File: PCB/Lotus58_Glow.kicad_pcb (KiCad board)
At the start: 2 copper layers, 139.1 x 107.7 mm, 133 parts, among them J1 PJ-320A, J2 Conn_01x02, P1 OLED, SW1 Kailh hotswap MX socket, SW10 Kailh hotswap MX socket, SW11 Kailh hotswap MX socket, SW12 Kailh hotswap MX socket, SW13 Kailh hotswap MX socket, SW14 Kailh hotswap MX socket, SW15 Kailh hotswap MX socket, SW16 Kailh hotswap MX socket, SW17 Kailh hotswap MX socket, SW18 Kailh hotswap MX socket, SW19 Kailh hotswap MX socket, SW2 Kailh hotswap MX socket, SW20 Kailh hotswap MX socket, SW21 Kailh hotswap MX socket, SW22 Kailh hotswap MX socket, SW23 Kailh hotswap MX socket, SW24 Kailh hotswap MX socket, SW25 Kailh hotswap MX socket, SW26 Kailh hotswap MX socket, SW27 Kailh hotswap MX socket, SW28 Kailh hotswap MX socket, SW29 Kailh hotswap MX socket, SW3 Kailh hotswap MX socket, SW30 Rotary_Encoder_Switch, SW31 Rotary_Encoder_Switch, SW4 Kailh hotswap MX socket, SW5 Kailh hotswap MX socket, SW6 Kailh hotswap MX socket, SW7 Kailh hotswap MX socket, SW8 Kailh hotswap MX socket, SW9 Kailh hotswap MX socket, U1 ProMicro

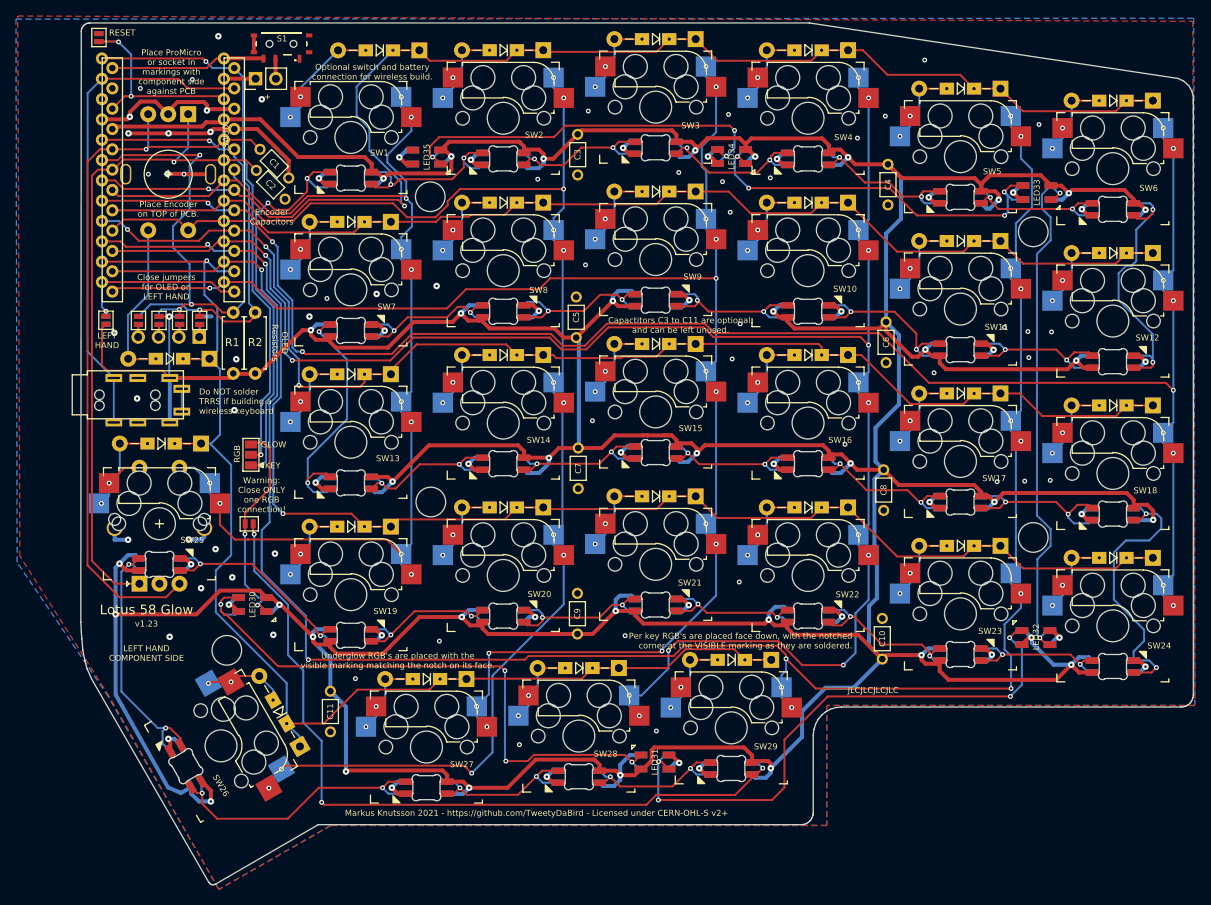
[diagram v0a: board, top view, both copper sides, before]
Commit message: Add mount holes for OLED cover
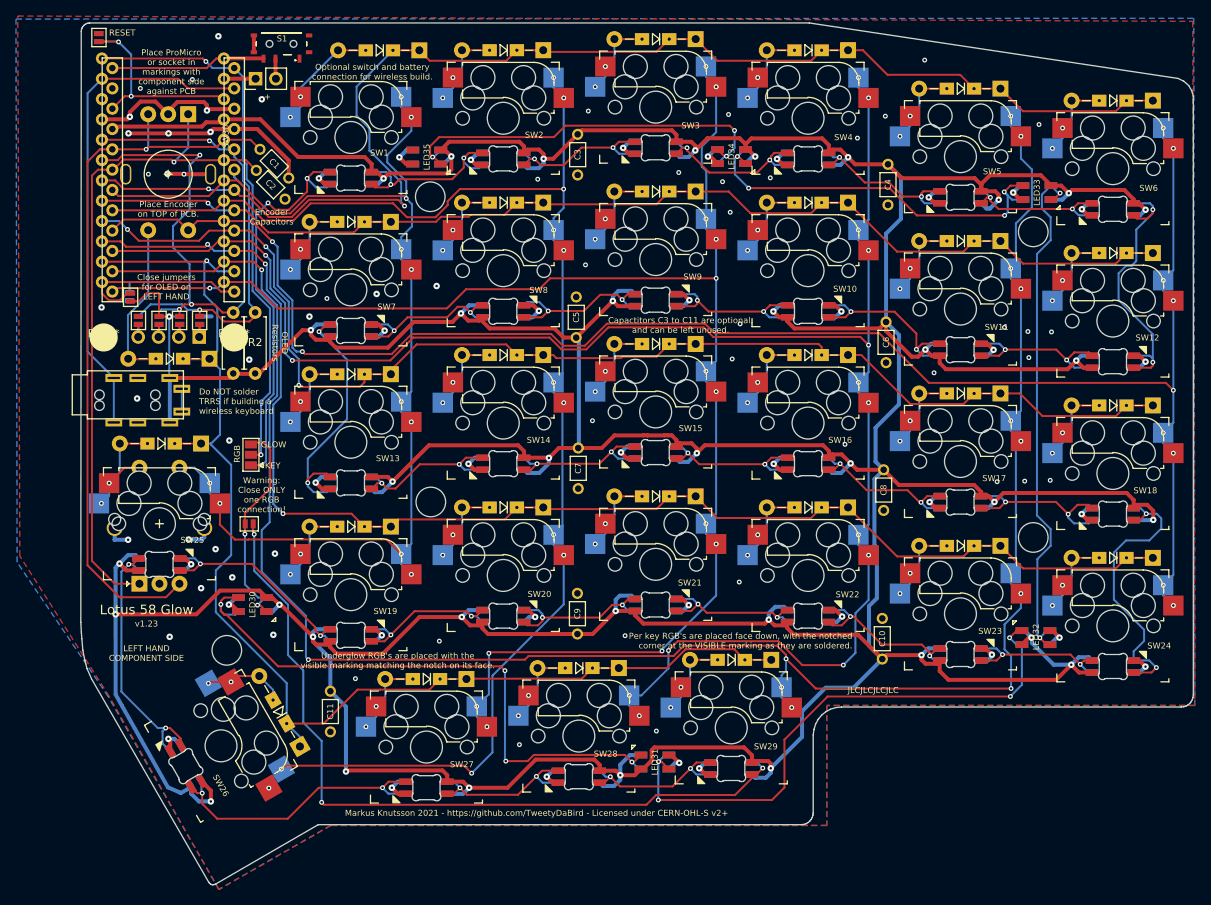
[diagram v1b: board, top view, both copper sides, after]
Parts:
- added REF**: Mount_M2, MountingHole:Mount_M2, F.Cu at (83.5, 75.0)
- added REF**: Mount_M2, MountingHole:Mount_M2, F.Cu at (99.8, 75.0)
- moved JP3 4.21 mm to (86.9, 70.0)
- moved JP4 4.17 mm to (86.7, 69.9)
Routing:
- net VCC: track 886.8 -> 879.1 mm
- net Hand: track 22.2 -> 27.5 mm, vias 1 -> 0
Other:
- net class Default removed
- net class GND removed
- net class VCC removed
- board text removed: "LEFT HAND"
- board text removed: "RIGHT HAND"
